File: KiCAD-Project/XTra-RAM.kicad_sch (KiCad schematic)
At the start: 32 parts, among them CN1 Bus_ISA_8bit, SW1 SW_DIP_x08, SW2 SW_DIP_x08, U1 AS6C4008-55PCN, U2 74LS245, U3 74LS151, U4 74LS151, U5 74LS157

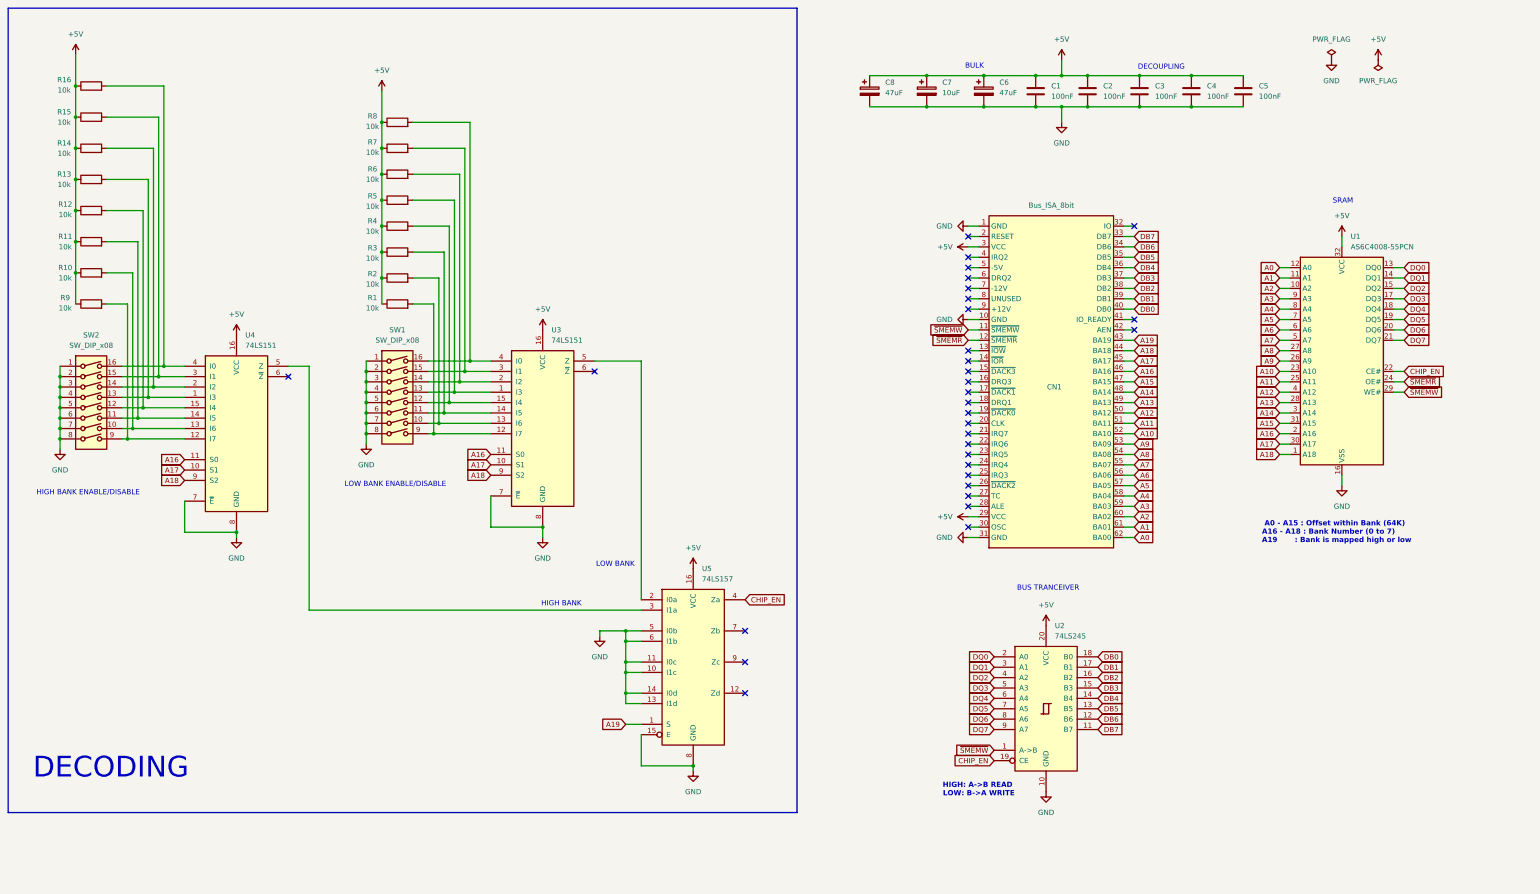
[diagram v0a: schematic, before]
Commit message: Minor updates to schematic diagrams
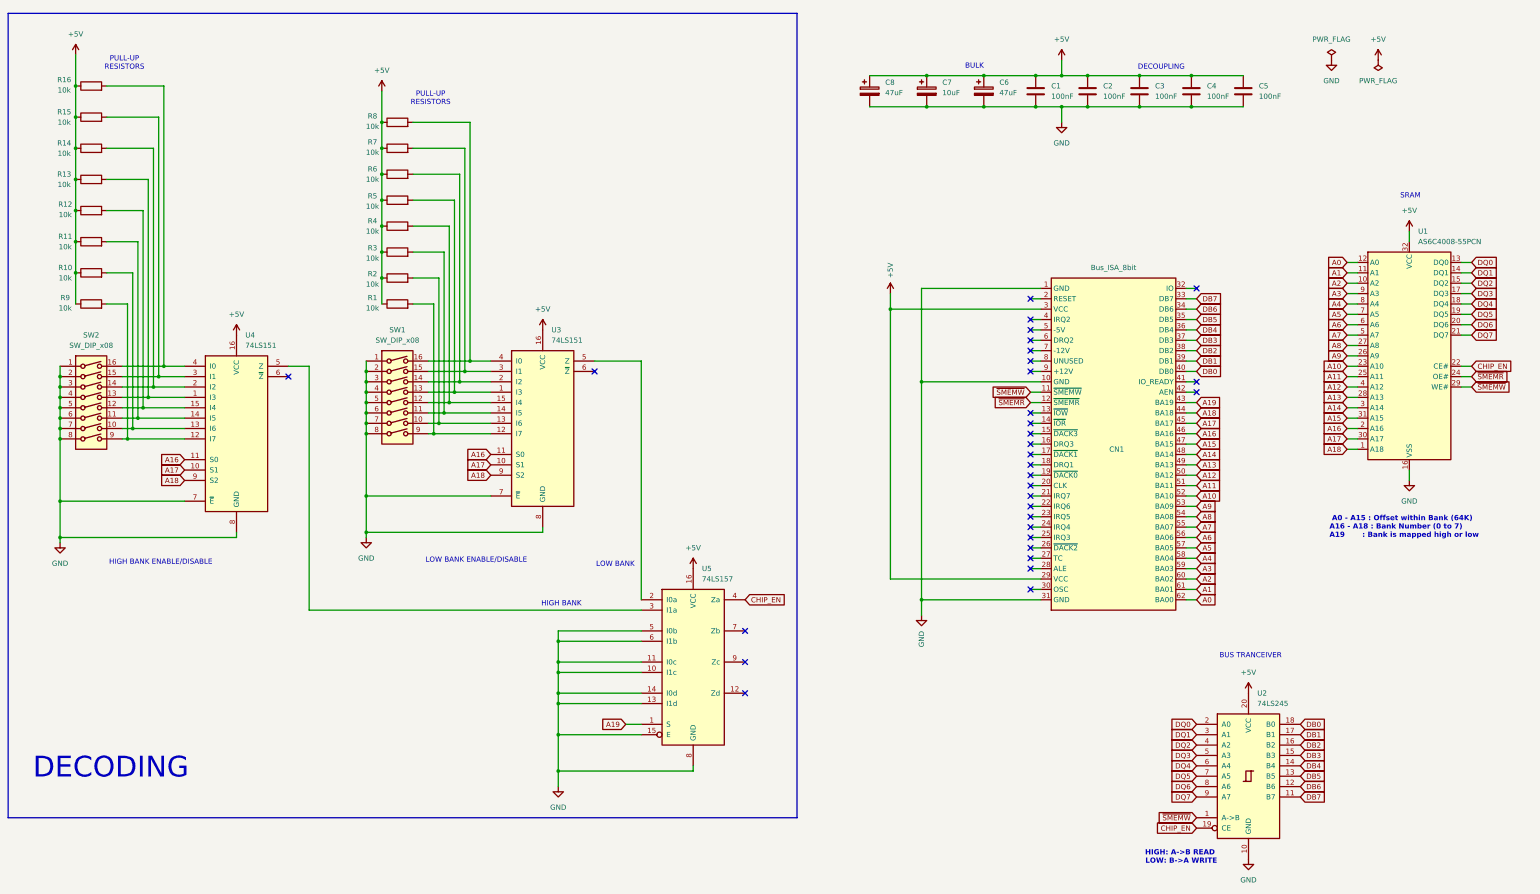
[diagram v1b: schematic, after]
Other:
- note added: "PULL-UP RESISTORS"
- company: b5s4 -> Oddsocks b5s4
- moved on the sheet: CN1, U1, U2
